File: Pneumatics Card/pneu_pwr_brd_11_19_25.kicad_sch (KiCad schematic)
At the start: 79 parts, among them J1 2X1, J10 Conn_01x02, J11 Conn_01x02, J12 2X1, J13 2X1, J2 2X1, J3 2X1, J4 2X1, J5 2X1, J6 2X1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

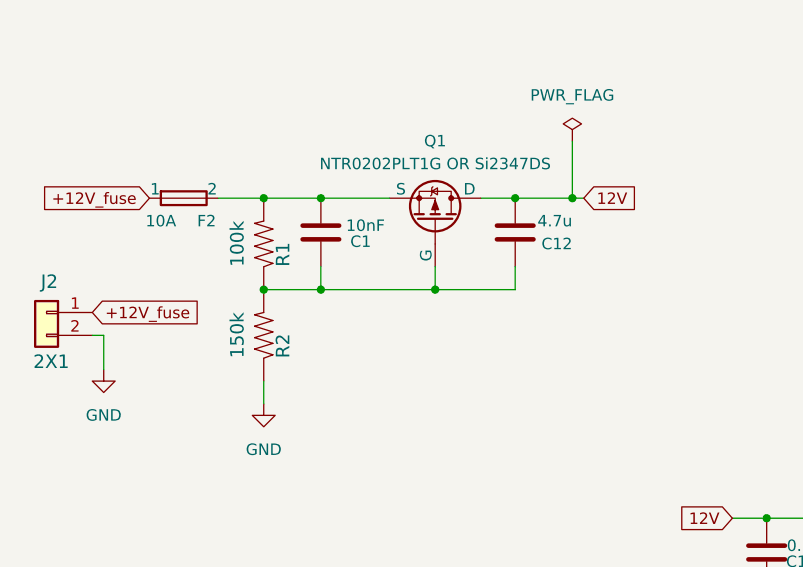
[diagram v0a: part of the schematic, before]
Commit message: Ramp rate values
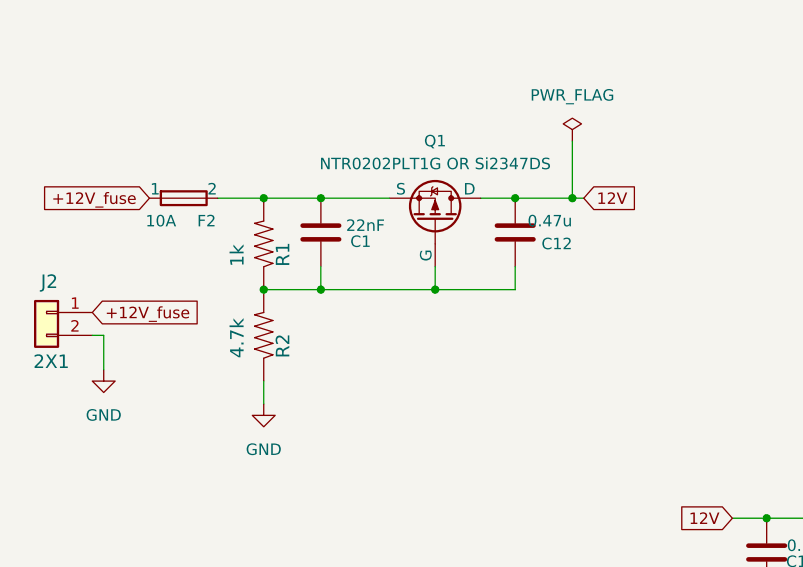
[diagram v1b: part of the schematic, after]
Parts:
- C1: value 10nF -> 22nF
- C12: value 4.7u -> 0.47u
- R1: value 100k -> 1k
- R2: value 150k -> 4.7k
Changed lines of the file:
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@@
 			)
 		)
-		(property "Value" "10nF"
+		(property "Value" "22nF"
 			(at 56.642 140.208 0)
 			(effects
@@
 			)
 		)
-		(property "Value" "150k"
+		(property "Value" "4.7k"
 			(at 39.37 154.94 0)
 			(effects
@@
 			)
 		)
-		(property "Value" "4.7u"
+		(property "Value" "0.47u"
 			(at 77.47 139.7 0)
 			(effects
@@
 			)
 		)
-		(property "Value" "100k"
+		(property "Value" "1k"
 			(at 39.37 144.78 0)
 			(effects

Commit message: Change the M3 hole
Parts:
- H1, H2, H3, H4: footprint MountingHole:MountingHole_4.3mm_M4_ISO7380_Pad_TopBottom -> MountingHole:MountingHole_3.2mm_M3_DIN965
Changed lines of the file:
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@@
 			)
 		)
-		(property "Footprint" "MountingHole:MountingHole_4.3mm_M4_ISO7380_Pad_TopBottom"
+		(property "Footprint" "MountingHole:MountingHole_3.2mm_M3_DIN965"
 			(at 43.18 298.45 0)
 			(effects
@@
 			)
 		)
-		(property "Footprint" "MountingHole:MountingHole_4.3mm_M4_ISO7380_Pad_TopBottom"
+		(property "Footprint" "MountingHole:MountingHole_3.2mm_M3_DIN965"
 			(at 43.18 290.83 0)
 			(effects
@@
 			)
 		)
-		(property "Footprint" "MountingHole:MountingHole_4.3mm_M4_ISO7380_Pad_TopBottom"
+		(property "Footprint" "MountingHole:MountingHole_3.2mm_M3_DIN965"
 			(at 43.18 312.42 0)
 			(effects
@@
 			)
 		)
-		(property "Footprint" "MountingHole:MountingHole_4.3mm_M4_ISO7380_Pad_TopBottom"
+		(property "Footprint" "MountingHole:MountingHole_3.2mm_M3_DIN965"
 			(at 43.18 304.8 0)
 			(effects

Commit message: old pneumatics
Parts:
- R1: value 1k -> 4.7k
- R2: value 4.7k -> 1k
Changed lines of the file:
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@@
 			)
 		)
-		(property "Value" "4.7k"
+		(property "Value" "1k"
 			(at 39.37 154.94 0)
 			(effects
@@
 			)
 		)
-		(property "Value" "1k"
+		(property "Value" "4.7k"
 			(at 39.37 144.78 0)
 			(effects

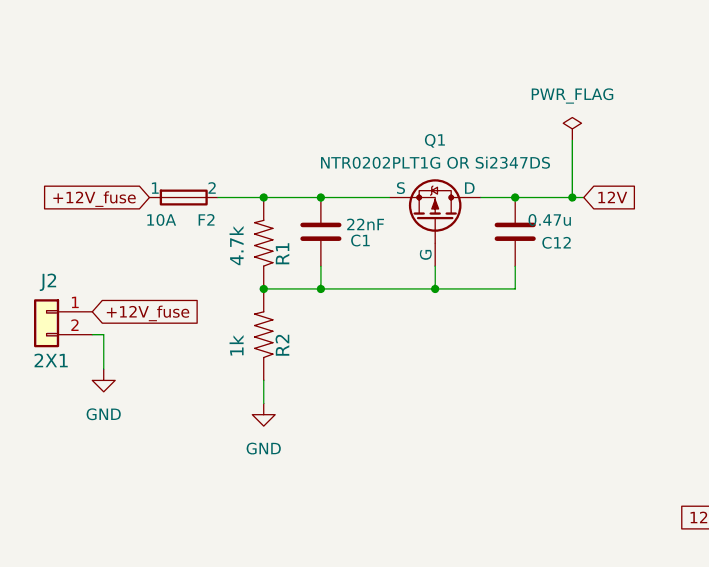
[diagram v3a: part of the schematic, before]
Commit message: Changed resistor values
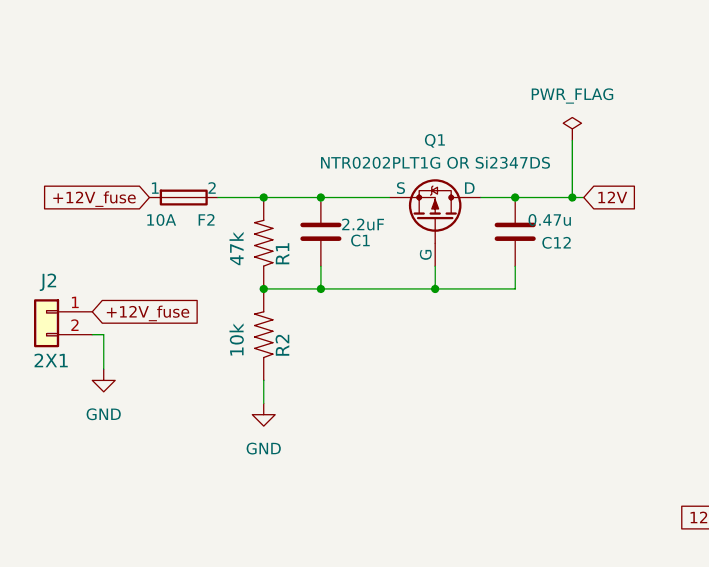
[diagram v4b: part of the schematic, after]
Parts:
- C1: value 22nF -> 2.2uF
- R1: value 4.7k -> 47k
- R2: value 1k -> 10k
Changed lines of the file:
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@@
 			)
 		)
-		(property "Value" "22nF"
+		(property "Value" "2.2uF"
 			(at 56.642 140.208 0)
 			(effects
@@
 			)
 		)
-		(property "Value" "1k"
+		(property "Value" "10k"
 			(at 39.37 154.94 0)
 			(effects
@@
 			)
 		)
-		(property "Value" "4.7k"
+		(property "Value" "47k"
 			(at 39.37 144.78 0)
 			(effects

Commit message: Fixed test points 3-1-2026
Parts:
- added 12V_TP1, 3.3V_TP_reg1, 3.3V_TP_stm1, 5V_TP1, GND_TP1, GND_TP2, S1_TP1, S1_out1, S2_TP1, S2_out1, S3_TP1, S3_out1, S4_TP1, S4_out1, SCL_ext1, SDA_ext1: TestPoint, Connector_PinHeader_1.00mm:PinHeader_1x01_P1.00mm_Vertical, symbol Connector:TestPoint
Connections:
- net USART+ is gone; now on net USART1_RX: J13.2 (Pin_2)
- net USART- is gone; now on net USART1_TX: J13.1 (Pin_1)
- net 12V: now also 12V_TP1.1
- net 3.3V: now also 3.3V_TP_reg1.1, 3.3V_TP_stm1.1
- net 5V: now also 5V_TP1.1
- net GND: now also GND_TP1.1, GND_TP2.1
- net S1CTRL: now also S1_TP1.1
- net S2CTRL: now also S2_TP1.1
- net S3CTRL: now also S3_TP1.1
- net S4CTRL: now also S4_TP1.1
- net SCL_ext: now also SCL_ext1.1
- net SDA_ext: now also SDA_ext1.1
- net at Q5.1 (G), R8.2, R9.2: now also S3_out1.1
- net at Q6.1 (G), R10.2, R11.2: now also S4_out1.1
- net at Q4.1 (G), R6.2, R7.2: now also S2_out1.1
- net at Q3.1 (G), R4.2, R5.2: now also S1_out1.1
- net USART1_TX: now reaches U6.25 (PC4)
- net USART1_RX: now reaches U6.26 (PC5)
- net USART1+: no longer names the net of U6.19 (PA2)
- net USART1-: no longer names the net of U6.20 (PA3)
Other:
- moved on the sheet: J13
